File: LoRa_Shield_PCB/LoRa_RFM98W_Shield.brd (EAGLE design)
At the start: 53.6 x 59.9 mm, 24 parts, among them IC1 AHT10, J2 TYPE-C-31-M-17, U1 RFM98W, U2 3V3_REG, U3 74HC4050, X2 BU-SMA-H

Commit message: PCB schematics almost complete, PCB layout partially done
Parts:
- removed JP6: (no value), pinhead_v2:1X04/OCT
- removed U3: 74HC4050, SparkFun-IC-Comms:SO16
- added C4, C5, C6: 100nF, rcl:C0603
- added IC2: TXS0102DCUR, SamacSys_Parts:SOP50P310X90-8N
- added R2, R3: 10k, rcl:R0603
- moved LED1 64.7 mm to (12.6, 14.0), turned to 0 degrees
- moved R1 62.8 mm to (14.2, 14.0), turned to 270 degrees
- moved IC1 55.9 mm to (24.6, 60.7), turned to 270 degrees
- moved SW1 32.5 mm to (25.1, 43.9), turned to 0 degrees
- moved J2 31.9 mm to (22.6, 15.2)
- moved C10 31.2 mm to (23.6, 34.5)
- moved U2 31.2 mm to (22.6, 29.0)
- moved D1 30.2 mm to (22.6, 20.3), turned to 0 degrees
- moved C1 27.1 mm to (22.6, 22.6), turned to 0 degrees
- moved JP5 23.9 mm to (43.4, 11.2)
- moved JP9 18.6 mm to (51.8, 45.0), turned to 180 degrees
- moved JP8 18.6 mm to (51.8, 47.0), turned to 180 degrees
- moved JP3 18.2 mm to (59.2, 36.6)
- moved B2 18.2 mm to (37.6, 39.1)
- moved JP1 18.2 mm to (16.0, 54.4)
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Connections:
- removed net N$31: B2.A4, JP4.2
- removed net N$32: B2.A5, JP4.1
- new net I2C_SCL_3V3: IC1.3, IC2.4, R2.1
- new net I2C_SCL_5V: B2.A5, IC2.1, JP4.1
- new net I2C_SDA_3V3: IC1.2, IC2.5, R3.1
- new net I2C_SDA_5V: B2.A4, IC2.8, JP4.2
- net 3.3V: now also C4.2, C5.1, IC1.4, IC2.3, IC2.6, R2.2, R3.2
- net 5V: now also C6.1, IC2.7
- net GND: now also C4.1, C5.2, C6.2, IC1.1, IC1.5, IC2.2
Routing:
- net N$2: track 10.2 -> 0.00 mm
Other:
- outline, holes or cut-outs redrawn

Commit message: update
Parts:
- moved C6 50.8 mm to (41.7, 21.3), turned to 90 degrees
- moved C5 44.9 mm to (38.6, 21.3), turned to 90 degrees
- moved JP8 15.0 mm to (36.8, 47.8)
- moved JP9 15.0 mm to (36.8, 45.7)
- moved R2 7.74 mm to (25.4, 54.4)
- moved R3 7.74 mm to (27.4, 54.4)
- moved C4 6.86 mm to (27.9, 59.7), turned to 0 degrees
- moved JP7 5.11 mm to (53.2, 57.7)
- moved U1 5.11 mm to (46.2, 46.5)
- moved X2 5.11 mm to (53.2, 64.0)
- moved C2 5.09 mm to (44.4, 57.1)
- moved C3 5.09 mm to (43.7, 59.7)
- moved IC1 3.97 mm to (27.2, 63.8), turned to 0 degrees
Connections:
- new net N$16: JP5.4
- new net N$8: JP5.3
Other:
- outline, holes or cut-outs redrawn

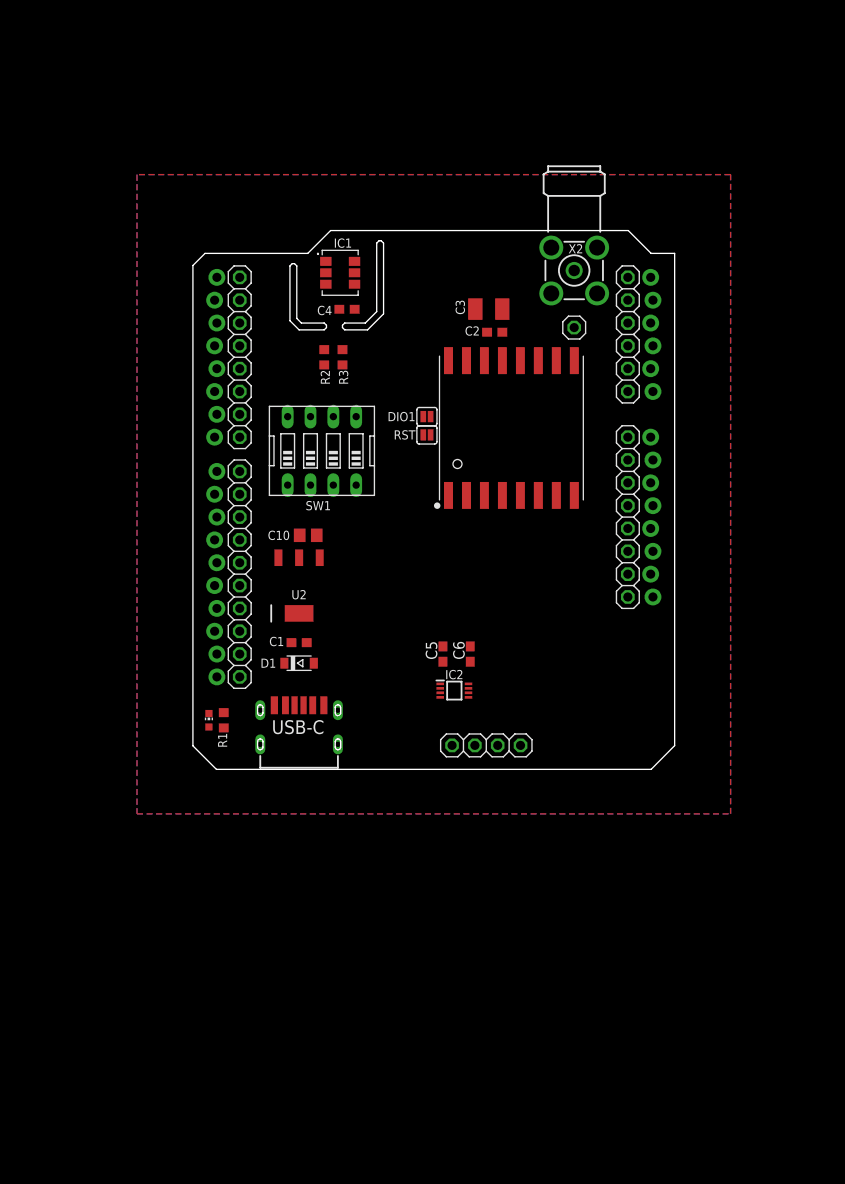
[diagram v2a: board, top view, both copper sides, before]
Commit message: ADC circuit, new PCB layout
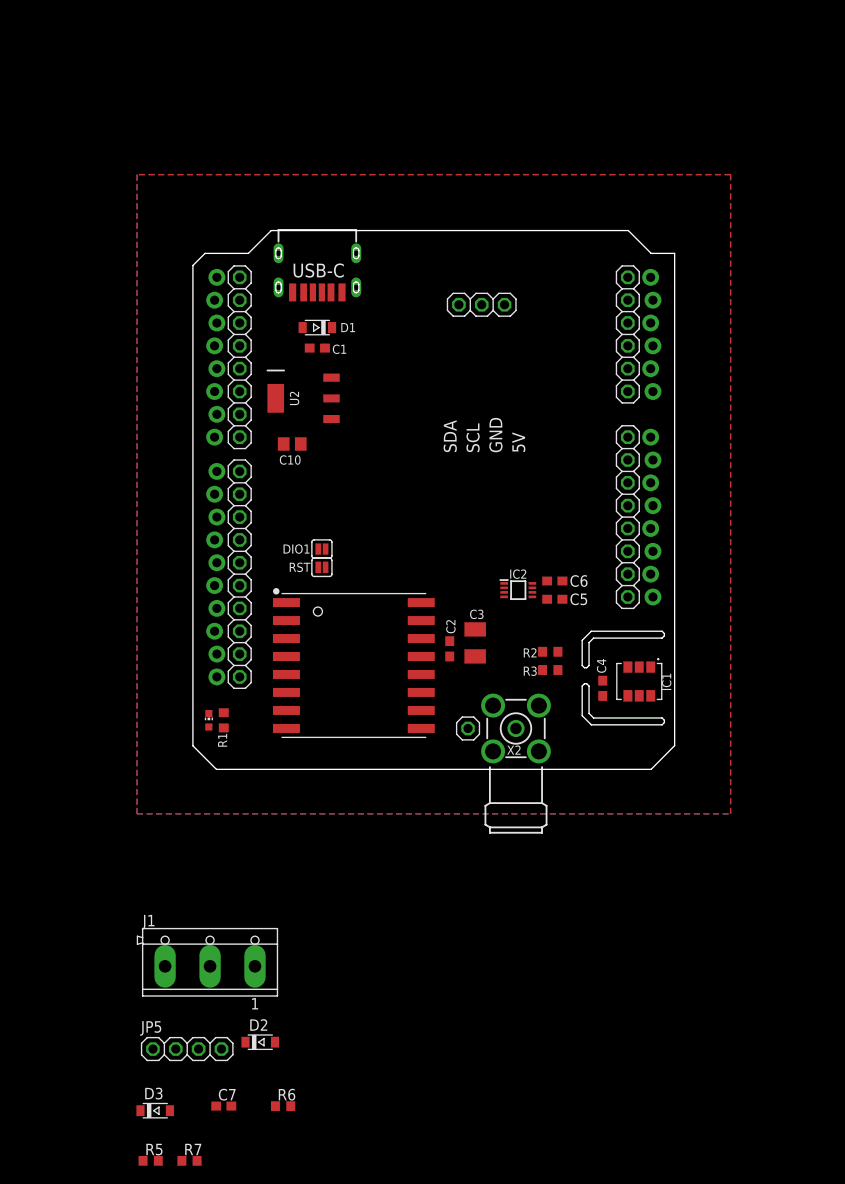
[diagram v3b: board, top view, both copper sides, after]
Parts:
- removed SW1: (no value), special:EDG-04
- added C7: 100nF, rcl:C0603
- added D2, D3: B5819W, dp_devices:SOD-123
- added J1: CON_TERMINAL_BLOCK_03-5MM, dp_devices:TERMINAL_BLOCK_3P_5
- added JP6: node number, pinhead_v2:1X03/OCT
- added R5, R7: 10k, rcl:R0603
- added R6: 150k, rcl:R0603
- JP5: value (none) -> OLED
- moved IC1 56.3 mm to (60.5, 18.3), turned to 270 degrees
- moved X2 51.4 mm to (46.7, 13.1), turned to 270 degrees
- moved C4 50.9 mm to (56.4, 17.5), turned to 270 degrees
- moved JP5 47.4 mm to (10.2, -22.6), turned to 0 degrees
- moved J2 46.8 mm to (24.6, 62.0), turned to 180 degrees
- moved JP7 46.1 mm to (41.4, 13.1), turned to 0 degrees
- moved R3 41.8 mm to (50.5, 19.6), turned to 180 degrees
- moved R2 41.3 mm to (50.5, 21.6), turned to 180 degrees
- moved D1 37.4 mm to (24.6, 57.7), turned to 180 degrees
- moved C3 37.2 mm to (42.2, 22.6), turned to 90 degrees
- moved C2 35.6 mm to (39.4, 21.9), turned to 90 degrees
- moved C1 32.8 mm to (24.6, 55.4), turned to 180 degrees
- moved U1 31.7 mm to (28.7, 20.1), turned to 0 degrees
- moved U2 20.8 mm to (23.1, 49.8), turned to 0 degrees
- moved JP8 18.8 mm to (25.1, 33.0)
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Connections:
- removed net N$16: JP5.4
- removed net N$27: B2.A0, JP4.6, SW1.4
- removed net N$28: B2.A1, JP4.5, SW1.3
- new net INPUT_RELAY_STATUS: B2.A1, J1.1, JP4.5, R5.2
- new net INPUT_VOLTAGE_READING: B2.A0, C7.1, D2.A, D3.C, JP4.6, R6.1, R7.2
- net 5V: now also D2.C, JP5.1
- net GND: now also C7.2, D3.A, J1.2, JP5.2, JP6.1, JP6.2, R5.1, R7.1; no longer SW1.5, SW1.6, SW1.7, SW1.8
- net I2C_SCL_5V: now also JP5.3
- net I2C_SDA_5V: now also JP5.4
- net N$29: no longer SW1.2
- net N$30: now also JP6.3; no longer SW1.1
- net N$8: now also J1.3, R6.2; no longer JP5.3
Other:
- outline, holes or cut-outs redrawn
- board text added: "5V"
- board text added: "GND"
- board text added: "SCL"
- board text added: "SDA"

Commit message: layout update
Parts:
- removed D2, D3: B5819W, dp_devices:SOD-123
- added D4: BAT54SWT1G, SamacSys_Parts:SOT65P220X100-3N
- added R10, R12, R8: 5k, rcl:R0603
- added R11, R4, R9: 10k, rcl:R0603
- R6: value 150k -> 165k
- R7: value 10k -> 15k
- moved R5 100.3 mm to (53.6, 53.3)
- moved R7 100.0 mm to (49.0, 57.1), turned to 180 degrees
- moved R6 89.5 mm to (45.2, 57.1), turned to 180 degrees
- moved C7 88.7 mm to (53.6, 50.5)
- moved J1 85.7 mm to (49.3, 64.5)
- moved JP5 61.2 mm to (32.8, 34.3)
- moved JP8 15.7 mm to (40.1, 28.4), turned to 0 degrees
- moved JP9 15.0 mm to (40.1, 30.5), turned to 0 degrees
- moved JP6 13.5 mm to (32.0, 52.3)
- moved LED1 1.37 mm to (13.8, 13.5)
- moved R1 1.37 mm to (15.5, 13.5)
- moved IC2 1.14 mm to (47.5, 27.4)
- moved C5 1.14 mm to (51.6, 26.4)
- moved C6 1.14 mm to (51.6, 28.4)
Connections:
- removed net SPI_CLK: B2.D13, JP2.5
- removed net SPI_MOSI: B2.D11, JP2.7, U1.MOSI
- removed net SPI_SCK: U1.SCK
- removed net SPI_SS: U1.NSS
- removed net SPI_SS_RFM: B2.D10, JP2.8
- new net SPI_CLK_3V3: R4.1, R8.2, U1.SCK
- new net SPI_CLK_5V: B2.D13, JP2.5, R8.1
- new net SPI_MOSI_3V3: R10.2, R9.1, U1.MOSI
- new net SPI_MOSI_5V: B2.D11, JP2.7, R10.1
- new net SPI_SS_RFM_3V3: R11.1, R12.2, U1.NSS
- new net SPI_SS_RFM_5V: B2.D10, JP2.8, R12.1
- net 5V: now also D4.2; no longer D2.C
- net GND: now also D4.1, R11.2, R4.2, R9.2; no longer D3.A
- net INPUT_VOLTAGE_READING: now also D4.3; no longer D2.A, D3.C

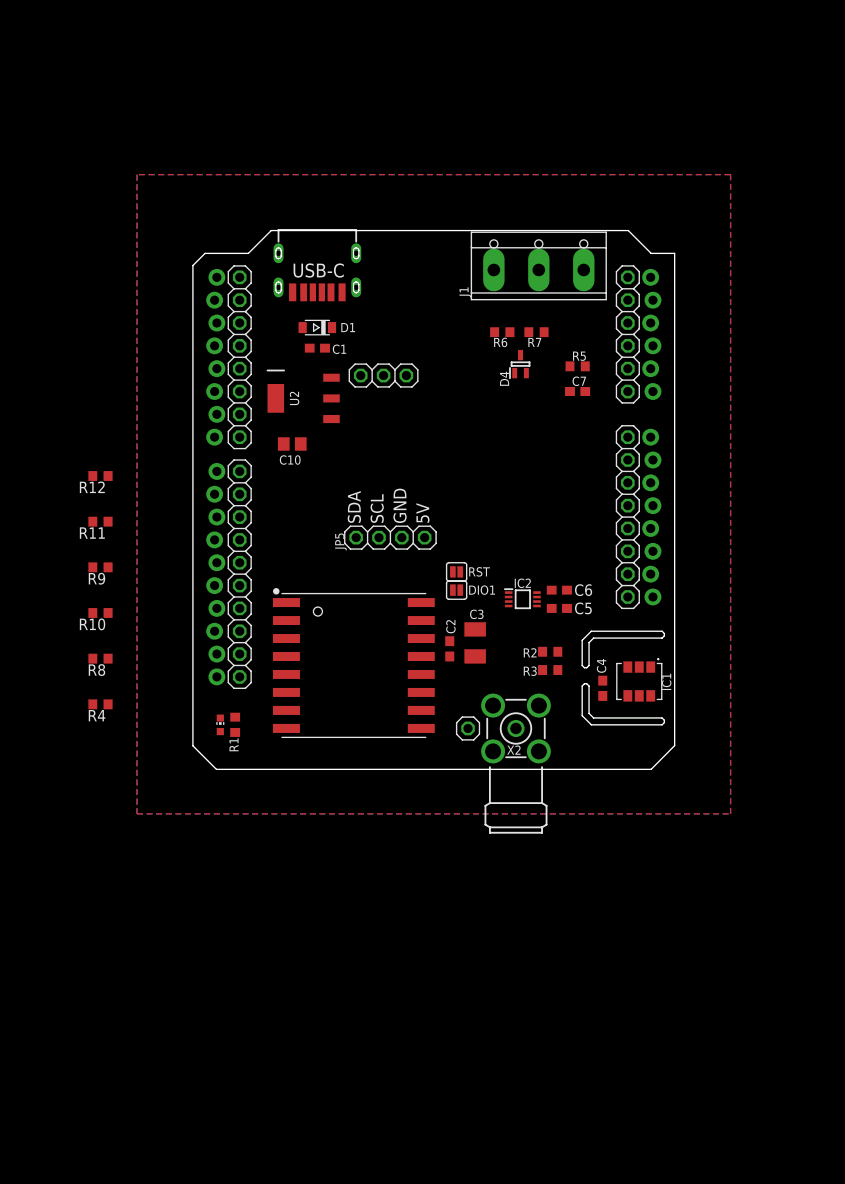
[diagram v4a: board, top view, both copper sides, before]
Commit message: schematics, layout update
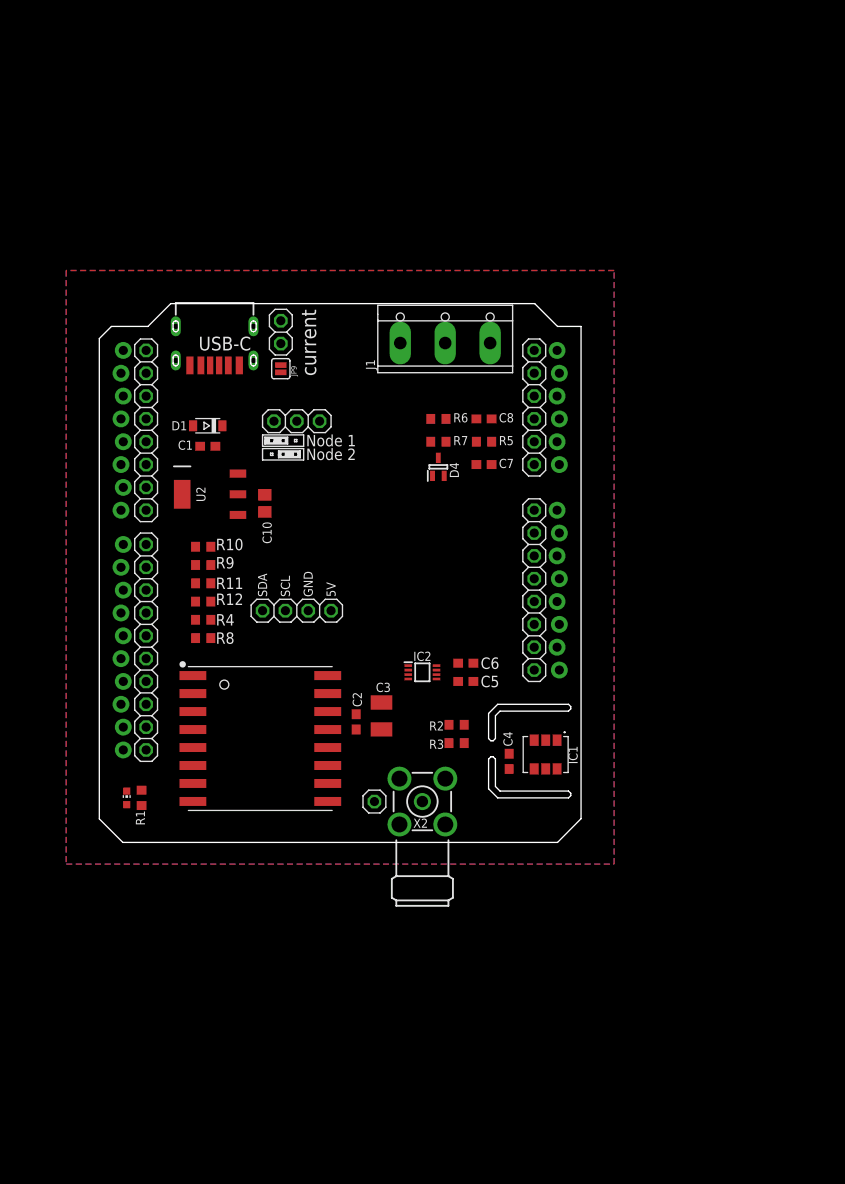
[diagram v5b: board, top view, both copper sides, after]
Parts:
- added C8: 100nF, rcl:C0603
- JP8: value JUMPER-SMT_2_NO_SILK -> current measurement; device SparkFun-Jumpers:SMT-JUMPER_2_NO_SILK -> pinhead_v2:1X02/OCT
- JP9: value JUMPER-SMT_2_NO_SILK -> JUMPER-SMT_2_NC_PASTE_SILK; device SparkFun-Jumpers:SMT-JUMPER_2_NO_SILK -> SparkFun-Jumpers:SMT-JUMPER_2_NC_PASTE_SILK
- moved JP8 34.7 mm to (20.6, 57.1), turned to 90 degrees
- moved JP9 29.9 mm to (20.6, 53.1), turned to 90 degrees
- moved R12 18.1 mm to (11.9, 27.2), turned to 0 degrees
- moved D1 16.4 mm to (12.4, 46.7)
- moved C1 16.4 mm to (12.4, 44.5)
- moved R7 16.4 mm to (38.1, 45.0)
- moved U2 14.9 mm to (12.7, 39.1)
- moved R4 14.8 mm to (11.9, 25.1)
- moved D4 14.6 mm to (38.1, 42.2)
- moved J2 14.0 mm to (13.2, 53.8)
- moved IC2 13.8 mm to (36.3, 19.3)
- moved R10 13.6 mm to (11.9, 33.3), turned to 0 degrees
- moved R5 13.4 mm to (43.2, 45.0)
- moved R11 13.3 mm to (11.9, 29.2)
- moved J1 13.2 mm to (38.9, 56.4)
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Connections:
- removed net N$11: B2.D5, JP1.3, JP9.1
- removed net N$9: B2.D3, JP1.5, JP8.1
- new net N$16: C1.1, D1.C, JP8.2, JP9.1
- net 5V: now also JP8.1, JP9.2; no longer C1.1, D1.C
- net GND: now also C8.1
- net INPUT_RELAY_STATUS: now also C8.2
- net RFM_DIO1: now also B2.D3, JP1.5; no longer JP8.2
- net RFM_RESET: now also B2.D5, JP1.3; no longer JP9.2
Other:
- outline, holes or cut-outs redrawn
- board text added: "Node 1"
- board text added: "Node 2"
- board text added: "current"
- board text removed: "DIO1"
- board text removed: "RST"

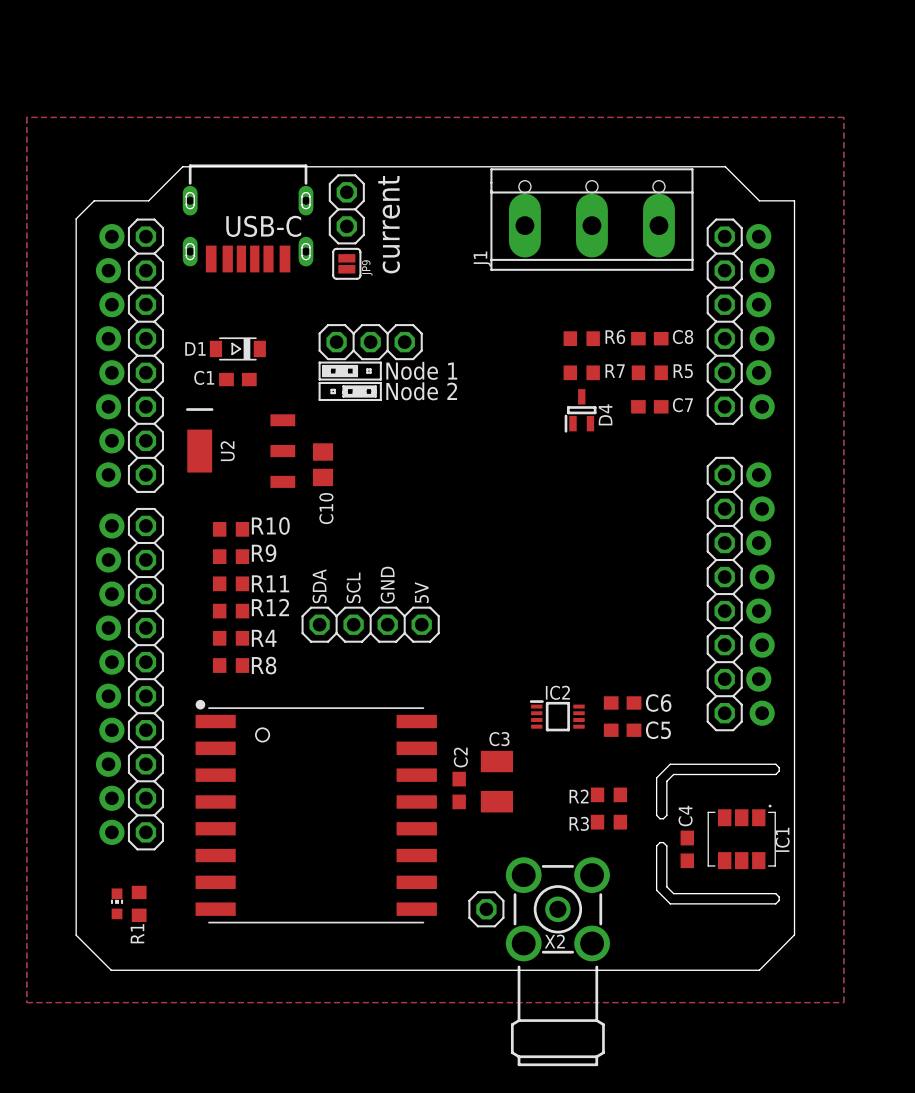
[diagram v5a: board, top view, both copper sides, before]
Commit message: PCB routing complete, RF impedance needs work
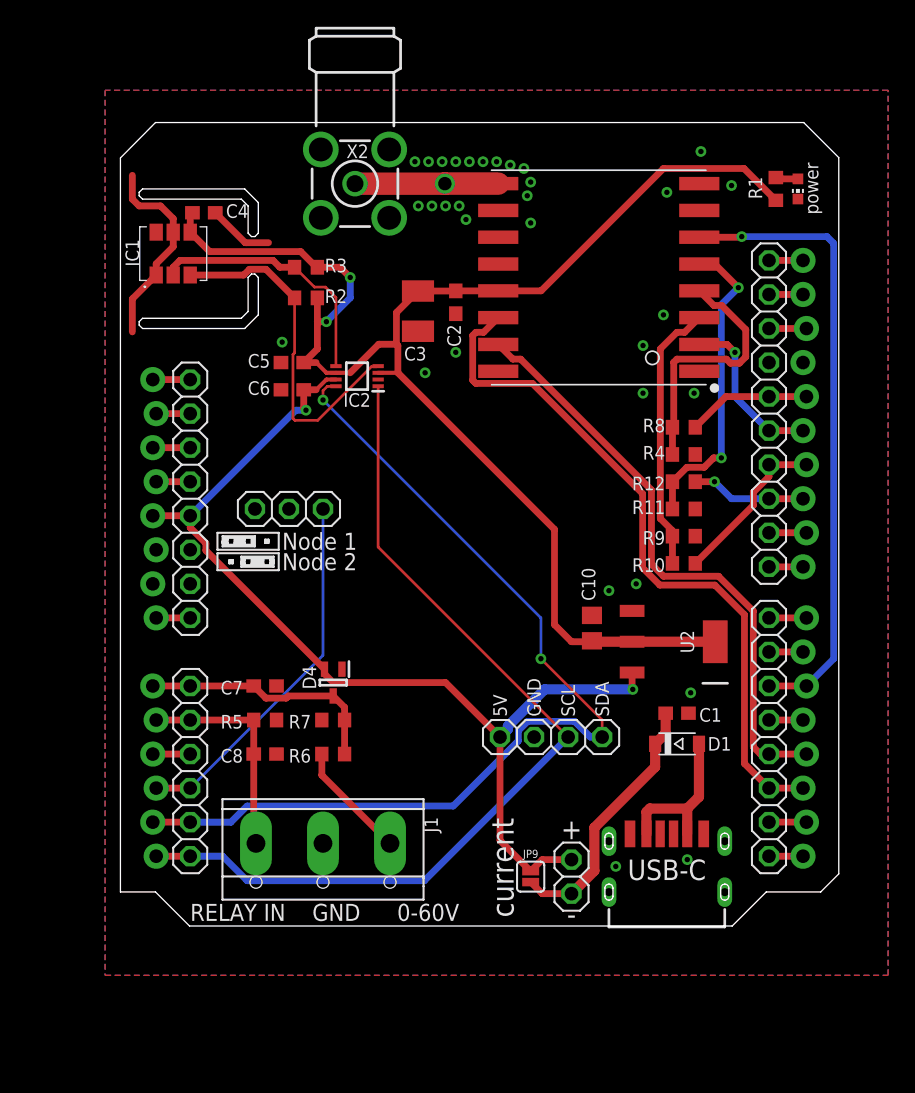
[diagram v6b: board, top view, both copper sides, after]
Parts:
- removed JP7: (no value), pinhead_v2:1X01/OCT
- moved LED1 73.7 mm to (54.2, 58.7), turned to 180 degrees
- moved R1 71.4 mm to (52.6, 58.7), turned to 90 degrees
- moved IC1 60.9 mm to (7.62, 53.8), turned to 90 degrees
- moved C4 59.6 mm to (9.91, 56.9), turned to 180 degrees
- moved X2 56.2 mm to (21.2, 59.1), turned to 90 degrees
- moved JP1 54.5 mm to (52.1, 17.8), turned to 270 degrees
- moved J2 53.7 mm to (44.5, 10.2), turned to 0 degrees
- moved JP8 52.5 mm to (37.3, 7.37), turned to 270 degrees
- moved JP4 52.1 mm to (8.89, 15.2), turned to 90 degrees
- moved J1 51.1 mm to (18.8, 9.40), turned to 180 degrees
- moved JP2 50.5 mm to (52.1, 41.9), turned to 270 degrees
- moved JP9 47.7 mm to (34.3, 7.37)
- moved R3 47.2 mm to (17.5, 52.8), turned to 0 degrees
- moved U1 45.3 mm to (39.4, 52.1), turned to 180 degrees
- moved D1 44.1 mm to (45.2, 17.3), turned to 0 degrees
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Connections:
- net N$2: no longer JP7.1
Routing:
- net 3.3V: track 0.00 -> 108.9 mm, vias 0 -> 2
- net 5V: track 0.00 -> 77.1 mm, vias 0 -> 2
- net I2C_SDA_5V: track 0.00 -> 73.1 mm, vias 0 -> 2
- net I2C_SCL_5V: track 0.00 -> 68.0 mm
- net RFM_DIO0: track 0.00 -> 52.8 mm
- net RFM_RESET: track 0.00 -> 46.9 mm, vias 0 -> 1
- net RFM_DIO1: track 0.00 -> 44.8 mm
- net N$30: track 0.00 -> 27.5 mm
- net I2C_SCL_3V3: track 0.00 -> 26.0 mm
- net SPI_SS_RFM_3V3: track 0.00 -> 23.3 mm, vias 0 -> 2
- net SPI_MOSI_3V3: track 0.00 -> 20.3 mm
- net GND: track 0.00 -> 20.0 mm, vias 0 -> 32
- net N$16: track 0.00 -> 19.8 mm
- net SPI_CLK_3V3: track 0.00 -> 19.4 mm
- net I2C_SDA_3V3: track 0.00 -> 19.2 mm
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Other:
- outline, holes or cut-outs redrawn
- board text added: "+"
- board text added: "-"
- board text added: "0-60V"
- board text added: "RELAY IN"
- board text added: "power"
